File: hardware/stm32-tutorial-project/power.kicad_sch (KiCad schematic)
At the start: 23 parts, among them J1 USB_C_Receptacle_USB2.0_14P, U2 AZ1117-3.3

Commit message: Add missing connectors, test points, and jumpers
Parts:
- JP2, JP3, JP6, JP7: footprint (none) -> Jumper:SolderJumper-2_P1.3mm_Open_Pad1.0x1.5mm
- TP3, TP4: footprint (none) -> TestPoint:TestPoint_Pad_D3.0mm
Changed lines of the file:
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@@
 			)
 		)
-		(property "Footprint" ""
+		(property "Footprint" "TestPoint:TestPoint_Pad_D3.0mm"
 			(at 151.13 96.52 0)
 			(effects
@@
 			)
 		)
-		(property "Footprint" ""
+		(property "Footprint" "Jumper:SolderJumper-2_P1.3mm_Open_Pad1.0x1.5mm"
 			(at 163.83 78.74 0)
 			(effects
@@
 			)
 		)
-		(property "Footprint" ""
+		(property "Footprint" "Jumper:SolderJumper-2_P1.3mm_Open_Pad1.0x1.5mm"
 			(at 205.74 90.17 0)
 			(effects
@@
 			)
 		)
-		(property "Footprint" ""
+		(property "Footprint" "Jumper:SolderJumper-2_P1.3mm_Open_Pad1.0x1.5mm"
 			(at 237.49 90.17 0)
 			(effects
@@
 			)
 		)
-		(property "Footprint" ""
+		(property "Footprint" "TestPoint:TestPoint_Pad_D3.0mm"
 			(at 95.25 68.58 0)
 			(effects
@@
 			)
 		)
-		(property "Footprint" ""
+		(property "Footprint" "Jumper:SolderJumper-2_P1.3mm_Open_Pad1.0x1.5mm"
 			(at 163.83 105.41 0)
 			(effects

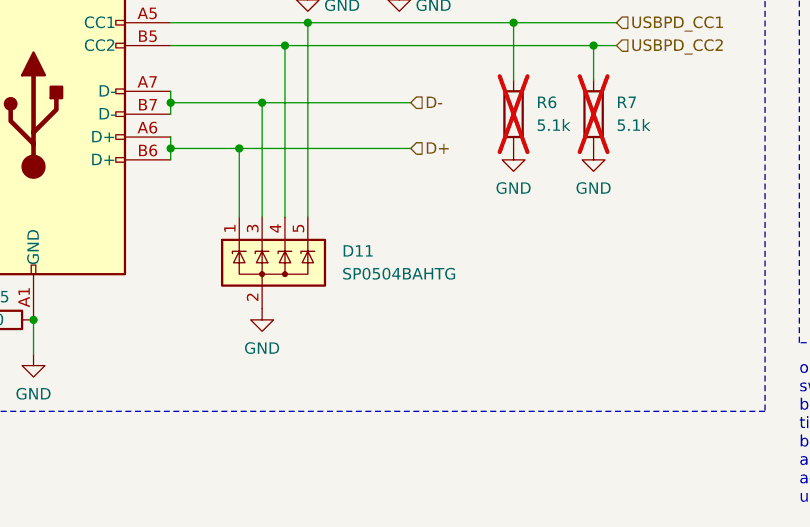
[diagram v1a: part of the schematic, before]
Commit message: now shows part number for the tvs diode
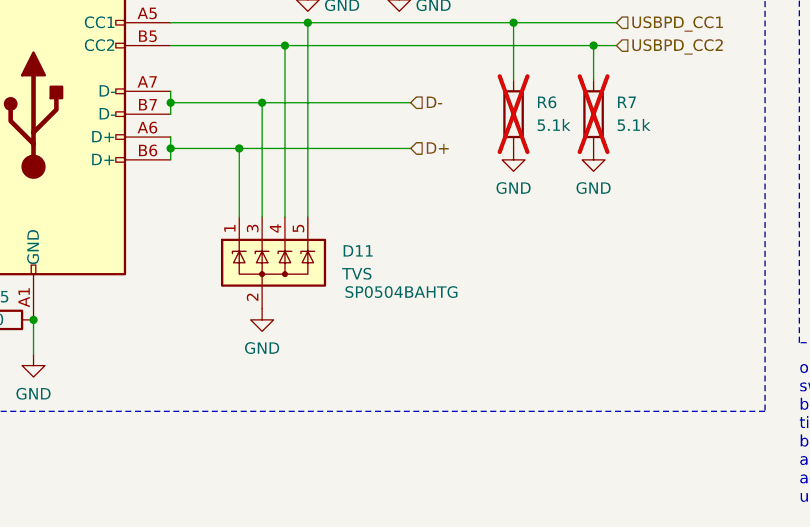
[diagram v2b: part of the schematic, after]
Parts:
- D11: value SP0504BAHTG -> TVS
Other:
- title: (none) -> POWER
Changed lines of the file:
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@@
 	(paper "A4")
 	(title_block
+		(title "POWER")
+		(date "2025-06-11")
 		(company "CAN source")
 	)
@@
 		(on_board yes)
 		(dnp no)
-		(fields_autoplaced yes)
 		(property "Reference" "D11"
 			(at 93.98 105.4099 0)
@@
 			)
 		)
-		(property "Value" "SP0504BAHTG"
+		(property "Value" "TVS"
 			(at 93.98 107.9499 0)
 			(effects
@@
 		)
 		(property "Part Number" "SP0504BAHTG"
-			(at 85.09 106.68 0)
-			(effects
-				(font
-					(size 1.27 1.27)
-				)
-				(hide yes)
-			)
-		)
+			(at 100.584 109.982 0)
+			(effects
+				(font
+					(size 1.27 1.27)
+				)
+			)
+		)
